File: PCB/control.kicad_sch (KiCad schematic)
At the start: 70 parts, among them SW8 SW_Push, U26 74LS00, U27 74LS04, U28 74LS04, U41 74LS161, U42 74LS138, U43 AT28C64B-15PU, U44 AT28C64B-15PU, U45 74LS00, U46 74LS04, U47 74LS04

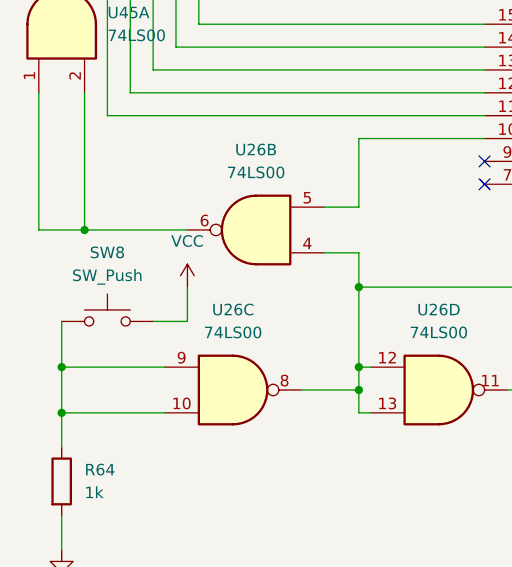
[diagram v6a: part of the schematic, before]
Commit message: update BOM to reflect cheaper prices and more acurate item ammounts, also worked on laying out the PCB.
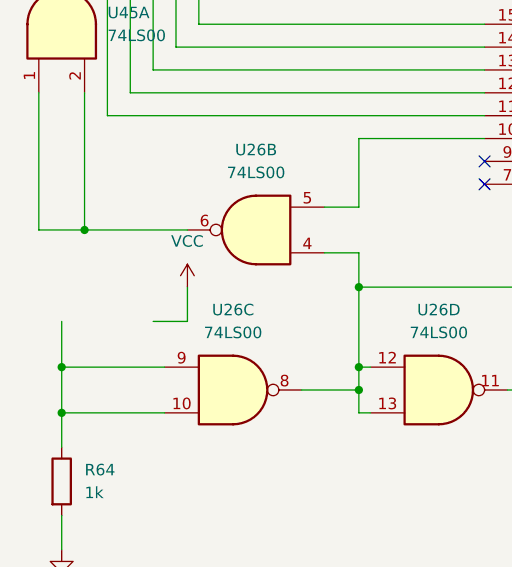
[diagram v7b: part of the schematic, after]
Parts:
- removed SW8: SW_Push, Button_Switch_THT:SW_PUSH_6mm, symbol Switch:SW_Push
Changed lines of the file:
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@@
-	)
-	(symbol
-		(lib_id "Switch:SW_Push")
-		(at 22.86 137.16 0)
-		(unit 1)
-		(exclude_from_sim no)
-		(in_bom yes)
-		(on_board yes)
-		(dnp no)
-		(fields_autoplaced yes)
-		(property "Reference" "SW8"
-			(at 22.86 129.54 0)
-			(effects
-				(font
-					(size 1.27 1.27)
-				)
-			)
-		)
-		(property "Value" "SW_Push"
-			(at 22.86 132.08 0)
-			(effects
-				(font
-					(size 1.27 1.27)
-				)
-			)
-		)
-		(property "Footprint" "Button_Switch_THT:SW_PUSH_6mm"
-			(at 22.86 132.08 0)
-			(effects
-				(font
-					(size 1.27 1.27)
-				)
-				(hide yes)
-			)
-		)
-		(property "Datasheet" "~"
-			(at 22.86 132.08 0)
-			(effects
-				(font
-					(size 1.27 1.27)
-				)
-				(hide yes)
-			)
-		)
-		(property "Description" "Push button switch, generic, two pins"
-			(at 22.86 137.16 0)
-			(effects
-				(font
-					(size 1.27 1.27)
-				)
-				(hide yes)
-			)
-		)
-		(pin "2"
-		)
-		(pin "1"
-		)
-		(instances
-			(project ""
-				(path "/48633dea-2de9-4b6f-aeff-2ee54233f918/d073e50d-b064-481f-8def-abf1072e09eb"
-					(reference "SW8")
-					(unit 1)
-				)
-			)
-		)
 	)
 	(symbol
